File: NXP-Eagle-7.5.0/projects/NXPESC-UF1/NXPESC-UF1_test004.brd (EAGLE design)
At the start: 59.7 x 34.5 mm, 88 parts, among them J1 ARM_MINI_JTAG-TH, P1 MOT_PWR_PAD-1, P15 DF13-6P-1.25H, P18 DF13-5P-1.25H, P2 MOT_PWR_PAD-1, P3 MOT_PWR_PAD-1, P4 MOT_PWR_PAD-1, P5 MOT_PWR_PAD-1, P8 DF13-4P-1.25H, P9 DF13-4P-1.25H, U1 74LVX14MTCX, U10 PSMN1R4-30YLD, U11 PSMN1R4-30YLD, U12 PSMN1R4-30YLD, U13 PSMN1R4-30YLD, U15 TJA1042TK/3, U2 MKV31F512VLH12-M, U8 PSMN1R4-30YLD, U9 PSMN1R4-30YLD

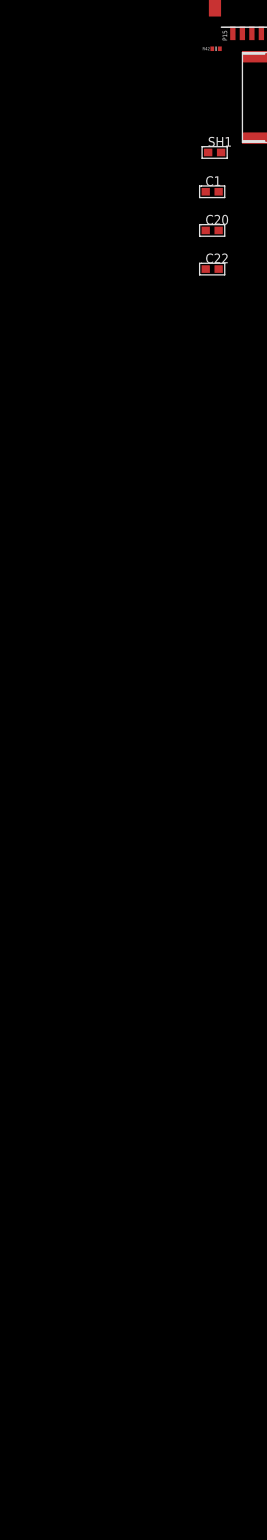
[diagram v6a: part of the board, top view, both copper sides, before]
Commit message: revisions. Adding MCU components, ESD protection, Thermister, oscillator, RGB LED, checking pinout. Moved CAN interface connection.
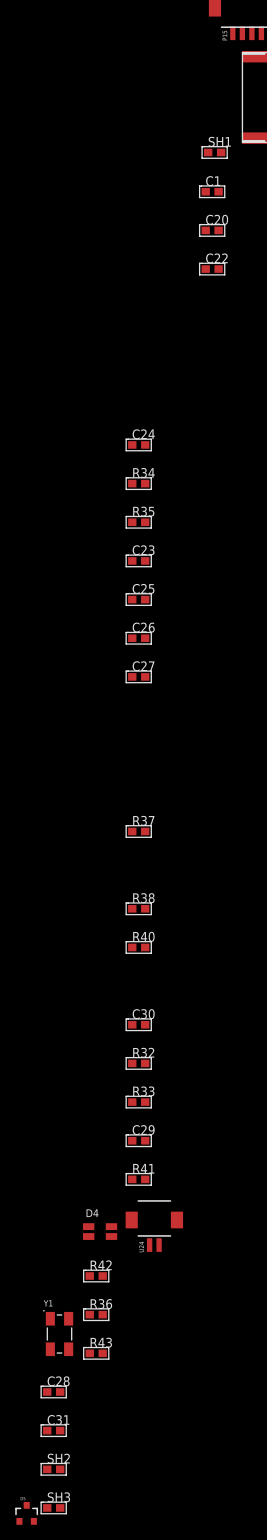
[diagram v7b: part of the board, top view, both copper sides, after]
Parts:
- added C23, C24, C25, C26, C30: CAP0603-0.1UF-25V, etc-rcl:C0603
- added C27, C29: CAP0603-2.2NF-25V, etc-rcl:C0603
- added C28, C31: CAP0603-15PF, etc-rcl:C0603
- added D4: CLV1A-FKB, CLV1A-FKB:4-PLCC
- added D5: PESD1CAN, PESD1CAN:SOT23-3
- added R32, R33: RESC0603-100R, etc-rcl:C0603
- added R34: RESC0603-1K-1, etc-rcl:C0603
- added R35, R40: RESC0603-10K-1, etc-rcl:C0603
- added R36, R37: RESC0603-270K-1, etc-rcl:C0603
- added R38, R41: RESC0603-4.99K-1, etc-rcl:C0603
- added R43: RESC0603-576R-1, etc-rcl:C0603
- added SH2, SH3: RESC0603-0R, etc-rcl:C0603
- added U24: DF13-2P-1.25H, pixhawk2:DF13A-2P-1.25H
- added Y1: ABM3B-8.000MHZ-B2-T, ABM3B-8.000MHZ-B2-T:OSCSC500X320X110-4N
- C1, C20, C21, C22: value CAP0603-1UF-50V -> CAP0603-0.1UF-50V
- R42: value (none) -> RESC0603-10K-1; device pixhawk2:0402-RES -> etc-rcl:C0603
- moved R42 162.1 mm to (-43.7, -144.3)
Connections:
- net N$25 renamed ENC_A_X
- net N$26 renamed ENC_B_X
- net N$27 renamed ENC_I_X
- net N$29 renamed ENC_A_IN
- net N$32 renamed ENC_B_IN
- net N$35 renamed ENC_I_IN
- removed net ENC_C: U1.12
- removed net VDDA: U2.13
- removed net VREFH: U2.14
- removed net VREFL: U2.15
- removed net VSSA: U2.16
- new net ADC1_DM1: C27.1, R33.1, U2.8
- new net ADC1_DP1: C29.1, R32.1, U2.7
- new net ENC_I: U1.12, U2.29
- new net EXTAL0: C28.1, U2.32, Y1.1
- new net LEDRGB-BLU/PTE25: R37.2, U2.60
- new net LEDRGB-GRN/PTD7: R36.2, U2.64
- new net LEDRGB-RED/PTD1: R43.2, U2.58
- new net N$25: D4.2, R42.2
- new net N$26: C30.2, R33.2, R41.2, U24.2
- new net N$27: C30.1, R32.2, R38.2, U24.1
- new net N$28: D4.3, R37.1
- new net N$29: D4.4, R36.1
- new net N$30: D4.1, R43.1
- new net N$31: SH3.2, U2.13, U2.14
- new net N$32: SH2.2, U2.15, U2.16
- new net N$8: U2.36
- new net VOLT_DCB/ADC0_SE13: C24.1, R34.2, R35.1, U2.38
- new net XTAL0: C31.1, U2.33, Y1.3
- net +3V3: now also C23.1, C26.1, R38.1, R42.1, SH3.1, U1.14
- net +5V: now also C25.1; no longer U1.14
- net +V_MOTOR: now also R35.2
- net AGND: now also R34.1
- net CAN0_RX: now also U2.21; no longer U2.29
- net CAN0_TX: now also U2.20; no longer U2.28
- net CANH: now also D5.1
- net CANL: now also D5.2
- net GND: now also C23.2, C24.2, C25.2, C26.2, C27.2, C28.2, C29.2, C31.2, D5.3, R41.1, SH2.1, Y1.2, Y1.4

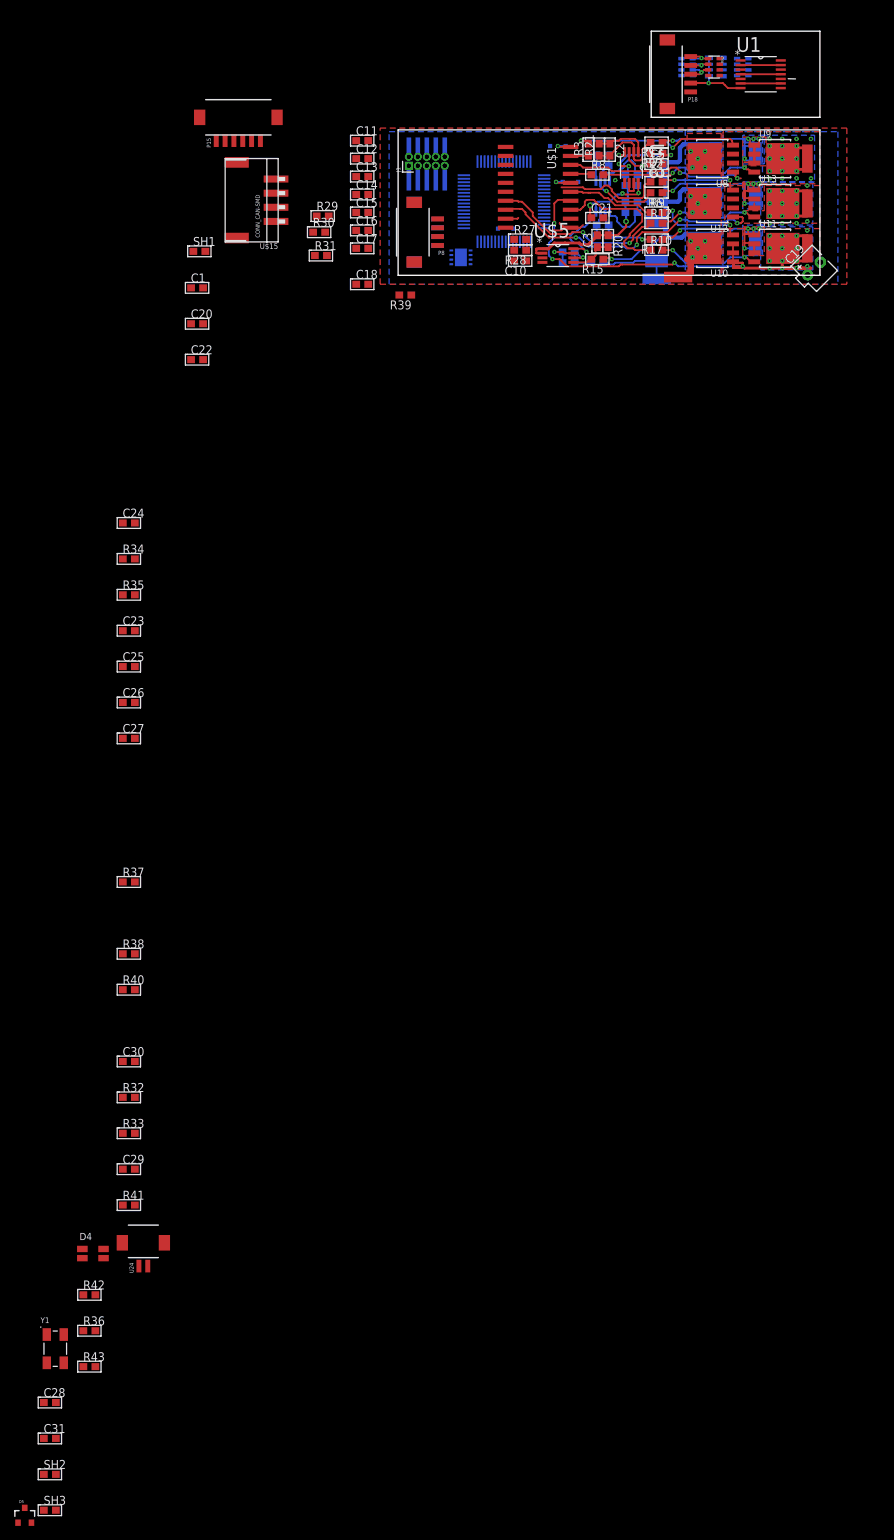
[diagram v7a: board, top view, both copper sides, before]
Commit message: Placing all new parts from schematic update. Looks tricky to fit everything onto this size board. Will likely need to make a bit bigger.
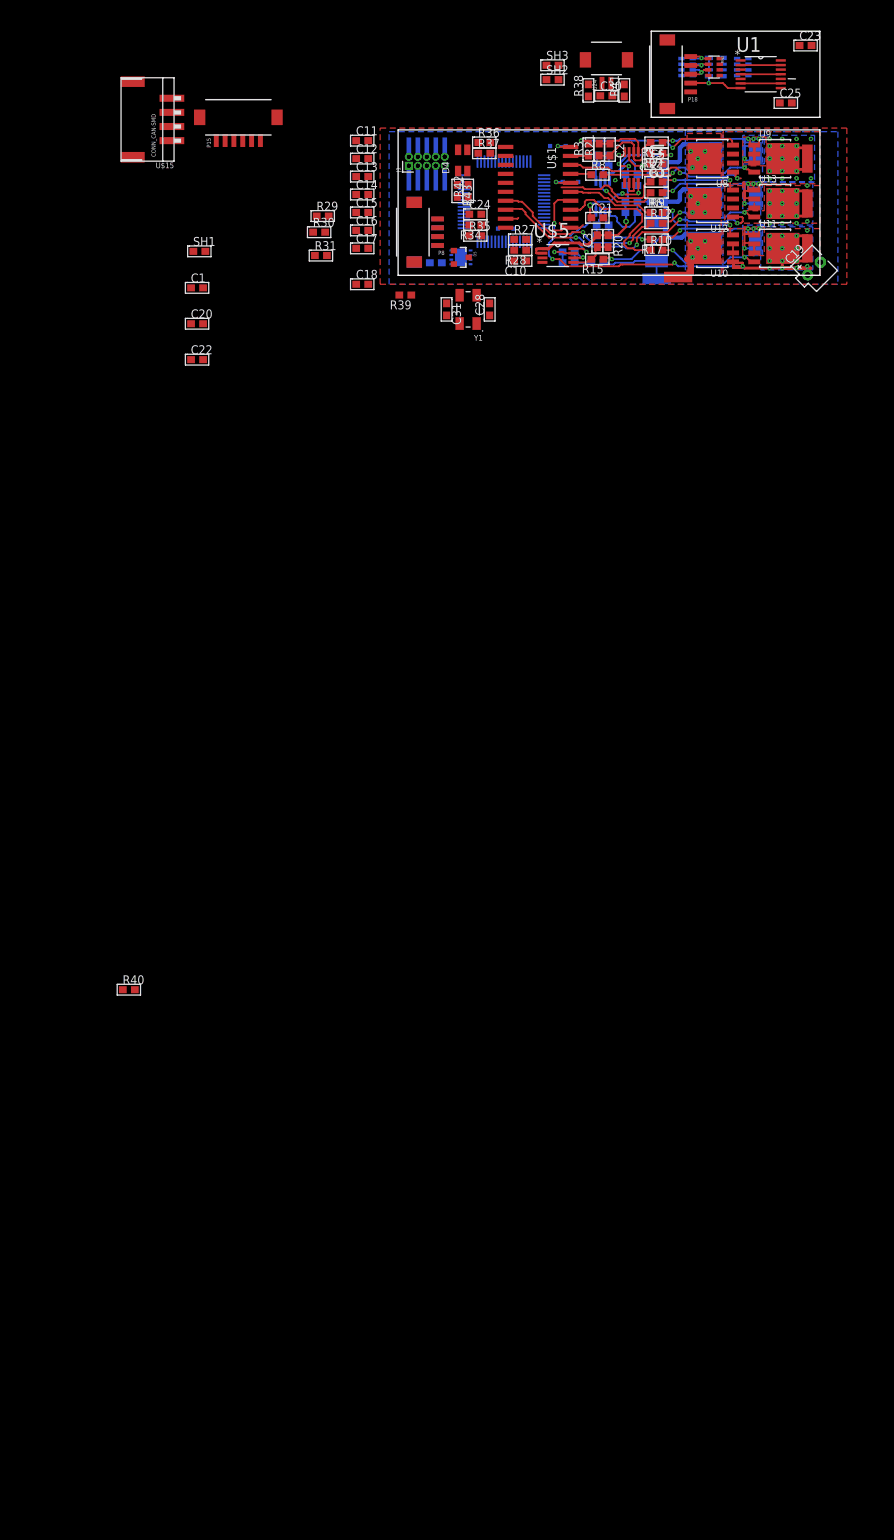
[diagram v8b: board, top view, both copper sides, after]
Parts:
- removed C27, C29: CAP0603-2.2NF-25V, etc-rcl:C0603
- removed R32, R33: RESC0603-100R, etc-rcl:C0603
- moved SH3 216.5 mm to (21.8, 29.7)
- moved SH2 209.8 mm to (21.8, 27.7)
- moved D5 188.4 mm to (8.89, 2.54), turned to 270 degrees
- moved U24 179.8 mm to (29.5, 30.5)
- moved R36 177.2 mm to (12.2, 18.8)
- moved R43 174.3 mm to (8.38, 11.9), turned to 270 degrees
- moved R41 172.6 mm to (32.0, 26.2), turned to 90 degrees
- moved C31 169.3 mm to (6.86, -4.83), turned to 270 degrees
- moved C28 166.7 mm to (13.0, -4.83), turned to 90 degrees
- moved R42 165.1 mm to (9.91, 11.9), turned to 90 degrees
- moved D4 163.3 mm to (9.14, 16.3), turned to 90 degrees
- moved Y1 158.2 mm to (9.91, -4.83), turned to 180 degrees
- moved C30 152.4 mm to (29.5, 25.4)
- moved R38 138.4 mm to (26.9, 26.2), turned to 90 degrees
- moved C23 126.6 mm to (57.7, 32.5)
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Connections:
- removed net N$26: C30.2, R33.2, R41.2, U24.2
- removed net N$27: C30.1, R32.2, R38.2, U24.1
- net ADC1_DM1: now also C30.2, R41.2, U24.2; no longer C27.1, R33.1
- net ADC1_DP1: now also C30.1, R38.2, U24.1; no longer C29.1, R32.1
- net GND: no longer C27.2, C29.2
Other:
- board text removed: "CAN Transceiver"
